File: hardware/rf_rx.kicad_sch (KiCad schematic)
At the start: 32 parts, among them J5 SMA_Conn, J6 Conn_Signal, J7 Conn_Amp1, J8 Conn_Amp2, J9 Conn_TriggerOut, Q1 BC847C,215, Q2 BC847C,215, U6 BA4584RF-E2, U7 MAX4003

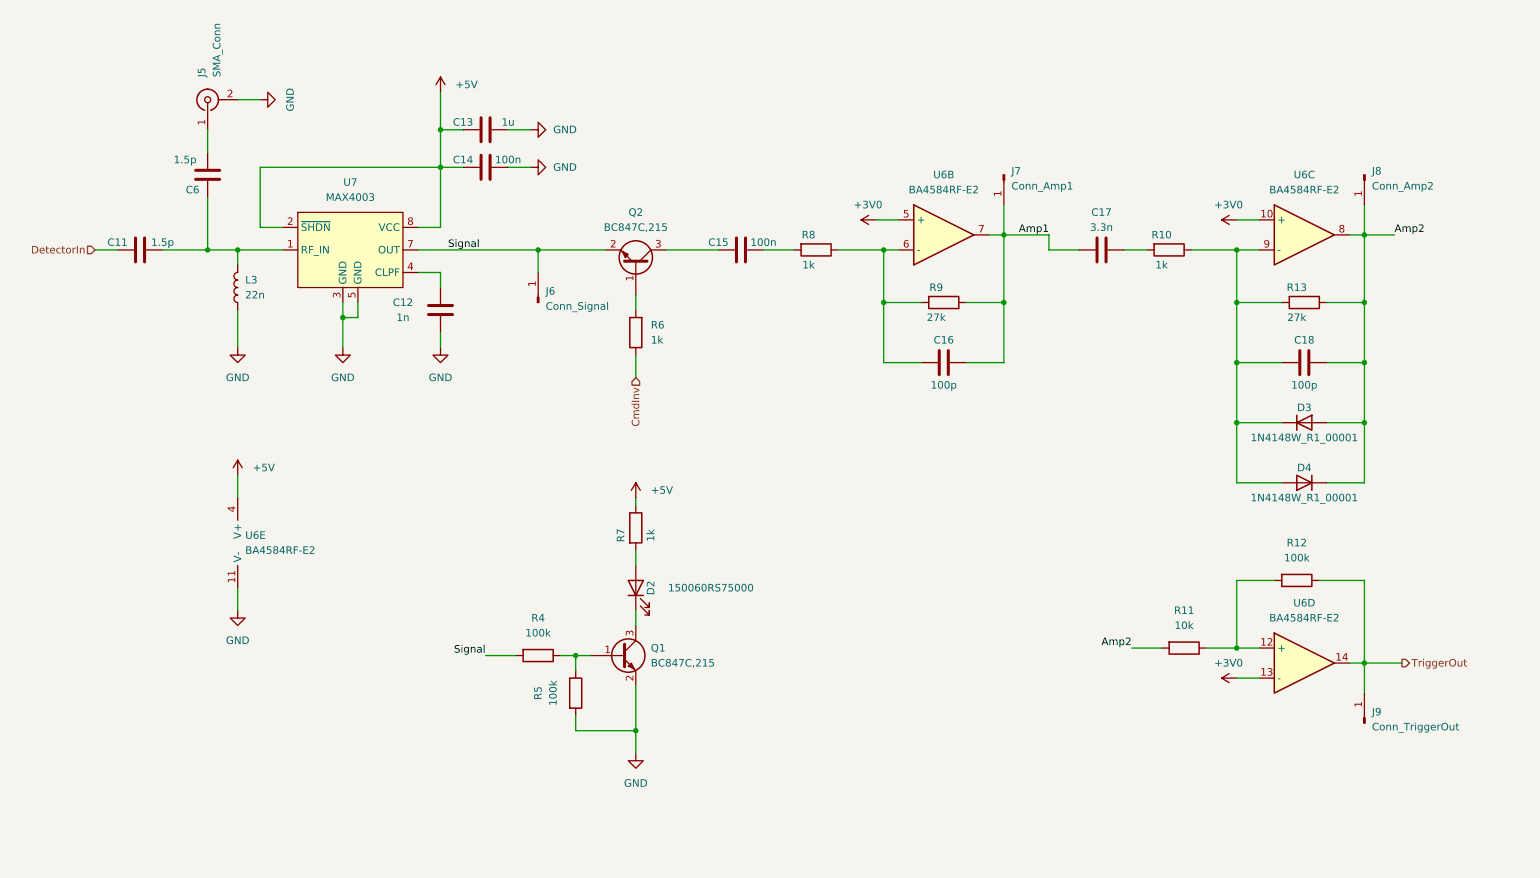
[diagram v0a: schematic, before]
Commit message: splitted quad opamp into dual opamp and comparator for better digitalization and smaller board
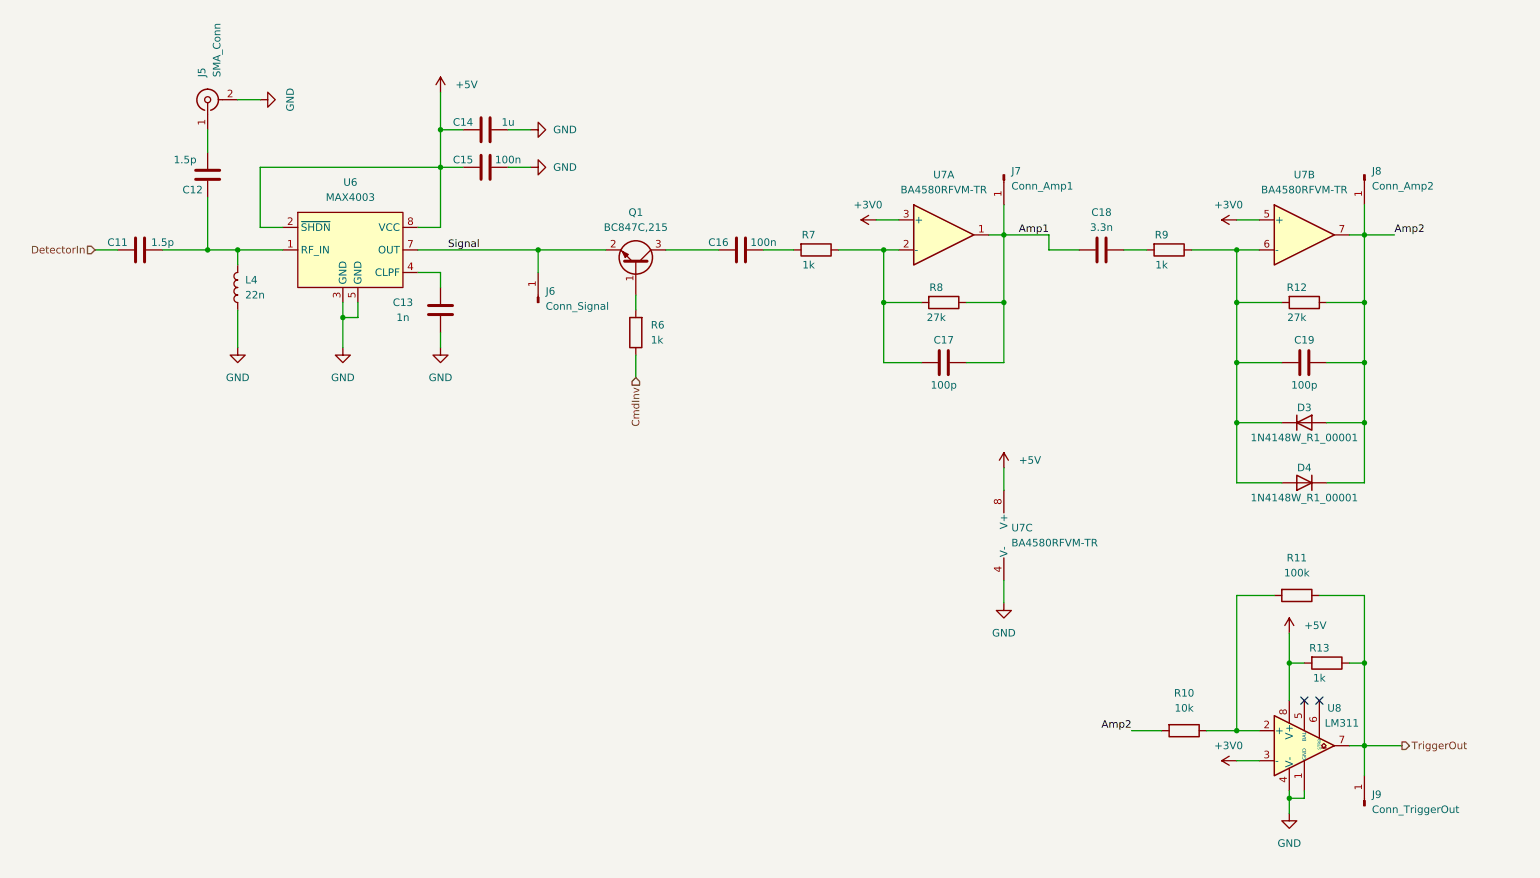
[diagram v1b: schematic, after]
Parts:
- removed D2: 150060RS75000, LED_SMD:LED_0603_1608Metric, symbol Device:LED
- removed Q1: BC847C,215, Package_TO_SOT_SMD:SOT-23, symbol Transistor_BJT:BC847
- removed R4, R5: 100k, Resistor_SMD:R_0603_1608Metric, symbol Device:R
- removed R7: 1k, Resistor_SMD:R_0603_1608Metric, symbol Device:R
- removed U6: BA4584RF-E2, Package_SO:SOIC-14_3.9x8.7mm_P1.27mm, symbol Device:Opamp_Quad
- added R13: 1k, Resistor_SMD:R_0603_1608Metric, symbol Device:R
- added U7: BA4580RFVM-TR, Package_SO:MSOP-8_3x3mm_P0.65mm, symbol Amplifier_Operational:LM358
- added U8: LM311, Package_SO:SOIC-8_3.9x4.9mm_P1.27mm, symbol Comparator:LM311
- renumbered C6 to C12, C12 to C13, C13 to C14, C14 to C15, C15 to C16, C16 to C17, C17 to C18, C18 to C19, L3 to L4, Q2 to Q1, R11 to R10, R12 to R11, R13 to R12, R8 to R7, R9 to R8, R10 to R9, U7 to U6
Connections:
- net +3V0: now also U7.3 (+), U7.5 (+), U8.3 (-)
- net +5V: now also R13.2, U7.8 (V+), U8.8 (V+)
- net Amp1: now also U7.1
- net Amp2: now also U7.7
- net GND: now also U7.4 (V-), U8.1 (GND), U8.4 (V-)
- net TriggerOut: now also R13.1, U8.7
- net at R10.1, R11.2: now also U8.2 (+)
- net at C19.2, D3.1 (K), D4.2 (A)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: now also U7.6 (-)
- net at C17.2, R7.1, R8.2: now also U7.2 (-)
- no-connect marks 0 -> 2
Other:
- moved on the sheet: J9, R10, R11

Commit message: Updated schematic, PCB and fabrication files
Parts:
- removed C19: 100p, Capacitor_SMD:C_0603_1608Metric, symbol Device:C
- removed D3, D4: 1N4148W_R1_00001, Diode_SMD:D_SOD-123, symbol Diode:1N4148W
- removed R12: 27k, Resistor_SMD:R_0603_1608Metric, symbol Device:R
- removed U7: BA4580RFVM-TR, Package_SO:MSOP-8_3x3mm_P0.65mm, symbol Amplifier_Operational:LM358
- added C22: 1u, Capacitor_SMD:C_0603_1608Metric, symbol Device:C
- added C24: 100n, Capacitor_SMD:C_0603_1608Metric, symbol Device:C
- added Q2: BC847C,215, Package_TO_SOT_SMD:SOT-23, symbol Transistor_BJT:BC847
- C20: renamed from C16; value 100n -> 10n
- C21: renamed from C17; value 100p -> 1n
- C23: renamed from C18; value 3.3n -> 100p
- J7: renamed from J8; value Conn_Amp2 -> Conn_CmdInv
- J8: renamed from J7; value Conn_Amp1 -> Conn_Amp
- R10: value 10k -> 6.2k
- R11: value 100k -> 220k
- R7, R9: value 1k -> 220k
- R8: value 27k -> 1k
- renumbered C11 to C15, C12 to C16, C13 to C17, C14 to C18, C15 to C19, L4 to L7, R13 to R12, U8 to U7
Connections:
- net +3V0 is gone; now on net Avr: U7.3 (-)
- net CmdInv: now also J7.1 (Pin_1)
- net GND: now also C23.2, C22.1, C24.1, Q2.2 (E)
- net Amp: now reaches C21.2, R7.1, R8.2
- net Amp: now also J8.1 (Pin_1), R10.2, R9.2, Q2.3 (C)
- net Avr: now reaches R9.1
- net Avr: now also C23.1
- net at C20.1, R7.2: now also Q2.1 (B)
- net +5V renamed +5VAnalog
- net +5VAnalog: now also C21.1, R8.1, C22.2; no longer R12.2, U7.8 (V+)
- removed net Amp1: C21.1, C23.2, J8.1 (Pin_1), R8.1
- removed net Amp2: J7.1 (Pin_1), R10.2
- new net +5VDigital: C24.2, R12.2, U7.8 (V+)
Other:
- moved on the sheet: C15, C16, C17, C18, C19, C20, C21, C23, J5, J6, J7, J8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

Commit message: changed R10 to 12k to increase tag pulse detection trigger threshold
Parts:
- R10: value 6.2k -> 12k
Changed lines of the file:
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@@
     (in_bom yes) (on_board yes)
     (property "Reference" "R10" (id 0) (at 222.25 76.2 90))
-    (property "Value" "6.2k" (id 1) (at 222.25 78.74 90))
+    (property "Value" "12k" (id 1) (at 222.25 78.74 90))
     (property "Footprint" "Resistor_SMD:R_0603_1608Metric" (id 2) (at 222.25 80.772 90)
       (effects (font (size 1.27 1.27)) hide)

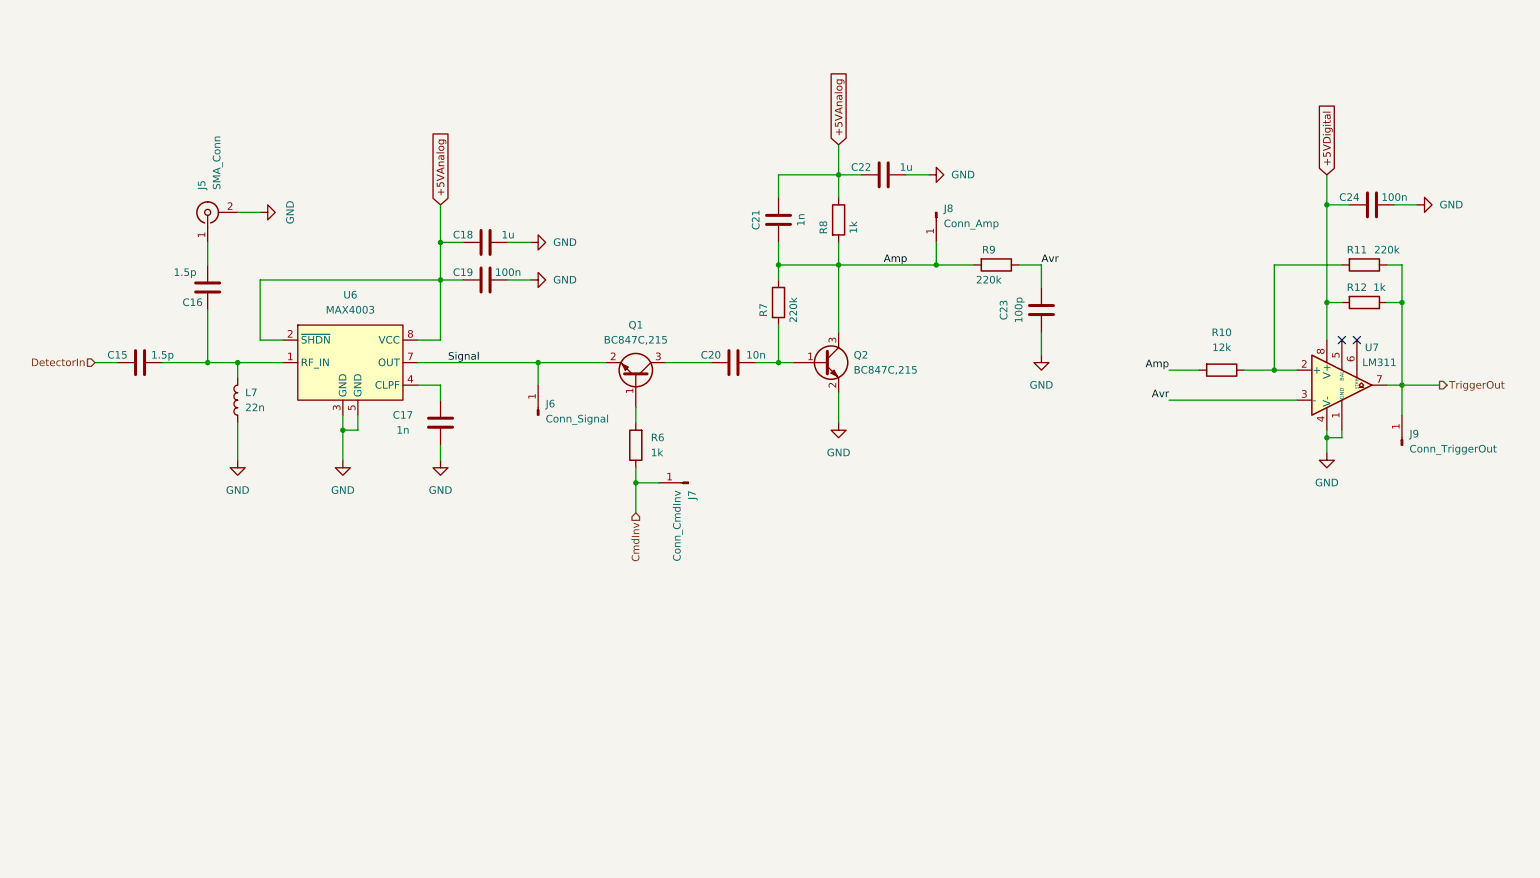
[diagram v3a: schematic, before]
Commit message: Rev 2. Using USB-C, configurable Tx, op-amp based LF amplifier, tri-color indicator. Using platformIO for firmware, splitted code into separate files.
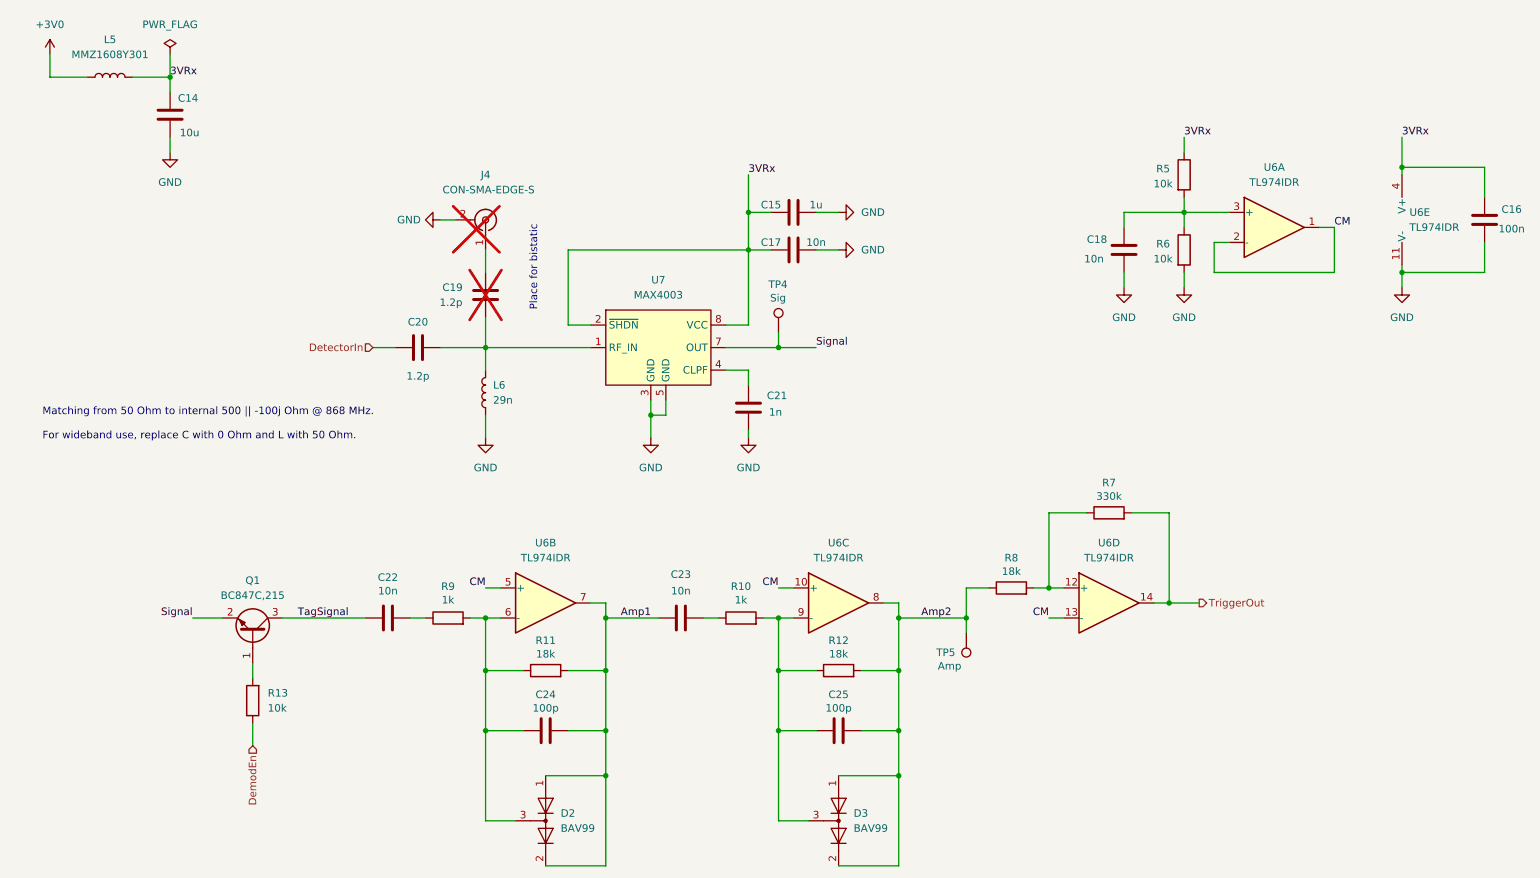
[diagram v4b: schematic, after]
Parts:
- removed C20: 10n, Capacitor_SMD:C_0603_1608Metric, symbol Device:C
- removed C21: 1n, Capacitor_SMD:C_0603_1608Metric, symbol Device:C
- removed J6: Conn_Signal, ProjLib:Single_Pin, symbol Connector:Conn_01x01_Male
- removed J7: Conn_CmdInv, ProjLib:Single_Pin, symbol Connector:Conn_01x01_Male
- removed J8: Conn_Amp, ProjLib:Single_Pin, symbol Connector:Conn_01x01_Male
- removed J9: Conn_TriggerOut, ProjLib:Single_Pin, symbol Connector:Conn_01x01_Male
- removed Q2: BC847C,215, Package_TO_SOT_SMD:SOT-23, symbol Transistor_BJT:BC847
- removed U7: LM311, Package_SO:SOIC-8_3.9x4.9mm_P1.27mm, symbol Comparator:LM311
- added C14: 10u, Capacitor_SMD:C_0603_1608Metric, symbol Device:C
- added C18: 10n, Capacitor_SMD:C_0603_1608Metric, symbol Device:C
- added C19: 1.2p, Capacitor_SMD:C_0603_1608Metric, symbol Device:C
- added C25: 100p, Capacitor_SMD:C_0603_1608Metric, symbol Device:C
- added D2, D3: BAV99, Package_TO_SOT_SMD:SOT-323_SC-70, symbol Diode:BAV99
- added L5: MMZ1608Y301, Inductor_SMD:L_0603_1608Metric, symbol Device:L
- added R5, R6: 10k, Resistor_SMD:R_0603_1608Metric, symbol Device:R
- added TP4: Sig, ProjLib:Single_Pin, symbol Connector:TestPoint
- added TP5: Amp, ProjLib:Single_Pin, symbol Connector:TestPoint
- added U6: TL974IDR, Package_SO:TSSOP-14_4.4x5mm_P0.65mm, symbol Amplifier_Operational:LM324
- C16: value 1.5p -> 100n; now in the parts list
- C17: renamed from C19; value 100n -> 10n
- C20: renamed from C15; value 1.5p -> 1.2p
- C22: value 1u -> 10n
- C23: value 100p -> 10n
- C24: value 100n -> 100p
- J4: renamed from J5; value SMA_Conn -> CON-SMA-EDGE-S; footprint Connector_Coaxial:SMA_Samtec_SMA-J-P-X-ST-EM1_EdgeMount -> Connector_Coaxial:SMA_Samtec_SMA-J-P-H-ST-EM1_EdgeMount; now not fitted; now left out of the parts list
- L6: renamed from L7; value 22n -> 29n
- R10: value 12k -> 1k
- R11: value 220k -> 18k
- R12, R8: value 1k -> 18k
- R13: renamed from R6; value 1k -> 10k
- R7: value 220k -> 330k
- R9: value 220k -> 1k
- U7: renamed from U6; footprint ProjLib:uMax-8 -> Package_SO:MSOP-8_3x3mm_P0.65mm
- renumbered C18 to C15, C17 to C21
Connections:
- net GND: now also C16.1, C14.1, C18.1, R6.2, U6.11 (V-); no longer C22.1, C23.2, C24.1
- net Signal: now also TP4.1
- net TriggerOut: now also R7.2, U6.14; no longer R11.1, R12.1
- net at J4.1 (In): now also C19.1; no longer C16.1
- net at C20.1, L6.2, U7.1 (RF_IN): now also C19.2; no longer C16.2
- net at R10.1: now also C23.1; no longer R11.2
- net TagSignal: now reaches Q1.3 (C)
- net TagSignal: now also C22.2
- net +5VAnalog renamed 3VRx
- net 3VRx: now also C16.2, C14.2, L5.2, R5.1, U6.4 (V+); no longer C22.2, R8.1
- net +5VDigital: no longer names the net of C24.2
- net +5VDigital: now also R11.1, R9.2, D2.3 (K), U6.6 (-); no longer R12.2
- net Amp: no longer names the net of R7.1, R8.2
- net Amp: now also U6.12 (+); no longer R10.2, R9.2
- net Avr: no longer names the net of R9.1
- net Avr: now also C22.1; no longer C23.1
- net CmdInv renamed DemodEn
- new net: C25.2, D3.3 (K), R10.2, R12.1, U6.9 (-)
- new net: C18.2, R5.2, R6.1, U6.3 (+)
- new net +3V0: L5.1
- new net Amp1: C23.2, C24.1, D2.1 (K), D2.2 (A), R11.2, U6.7
- new net Amp2: C25.1, D3.1 (K), D3.2 (A), R12.2, R8.1, TP5.1, U6.8
- new net CM: U6.1, U6.10 (+), U6.13 (-), U6.2 (-), U6.5 (+)
- no-connect marks 2 -> 0
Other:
- note added: "Matching from 50 Ohm to internal 500 || -100j Ohm @ 868 MHz. For wideband use, replace C with 0 Ohm and L with 50 Ohm."
- note added: "Place for bistatic"
- moved on the sheet: C15, C17, C20, C21, L6, R13, U7
